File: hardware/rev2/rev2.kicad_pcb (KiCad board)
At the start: 4 copper layers, 60 x 40 mm, 154 parts, among them J1 USB_C_Receptacle_USB2.0_16P, J2 uFL, J3 uFL, J4 Antenna RF and GNSS Data, J5 Antenna GND, J6 uFL, J7 uFL, J8 Battery Connection, Q1 SS8050, SW1 SW_Push, SW2 SW_Push, U1 EClamp2522P, U2 ESP32-S3FN8, U3 SX1262IMLTRT, U4 PE4259, U5 MP2664GG-xxxx-P, U6 MAX17055ETB+, U8 TPS631000DRLR, Y1 ECS-2520SMV-400-FN-TR, Y2 TXO-20CSMV-320

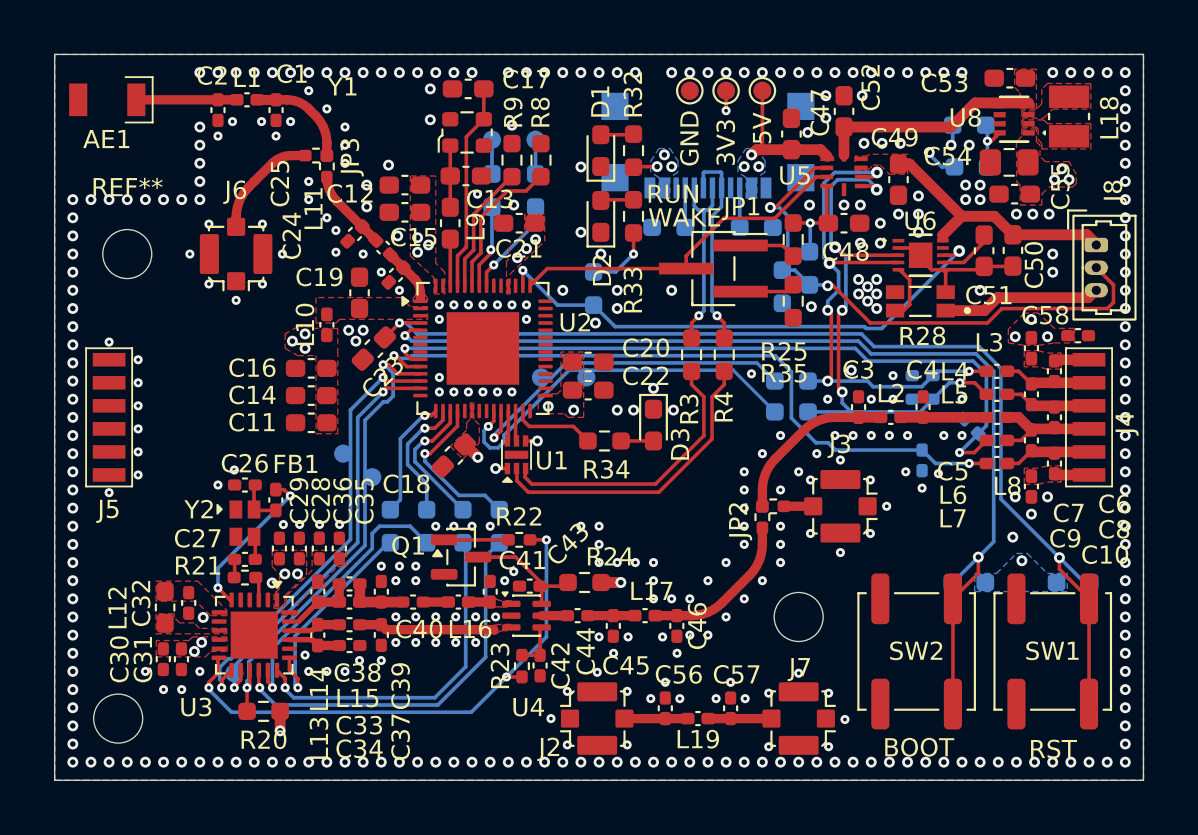
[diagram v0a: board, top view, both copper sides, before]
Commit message: fixed soldermask and silkscreen mostly
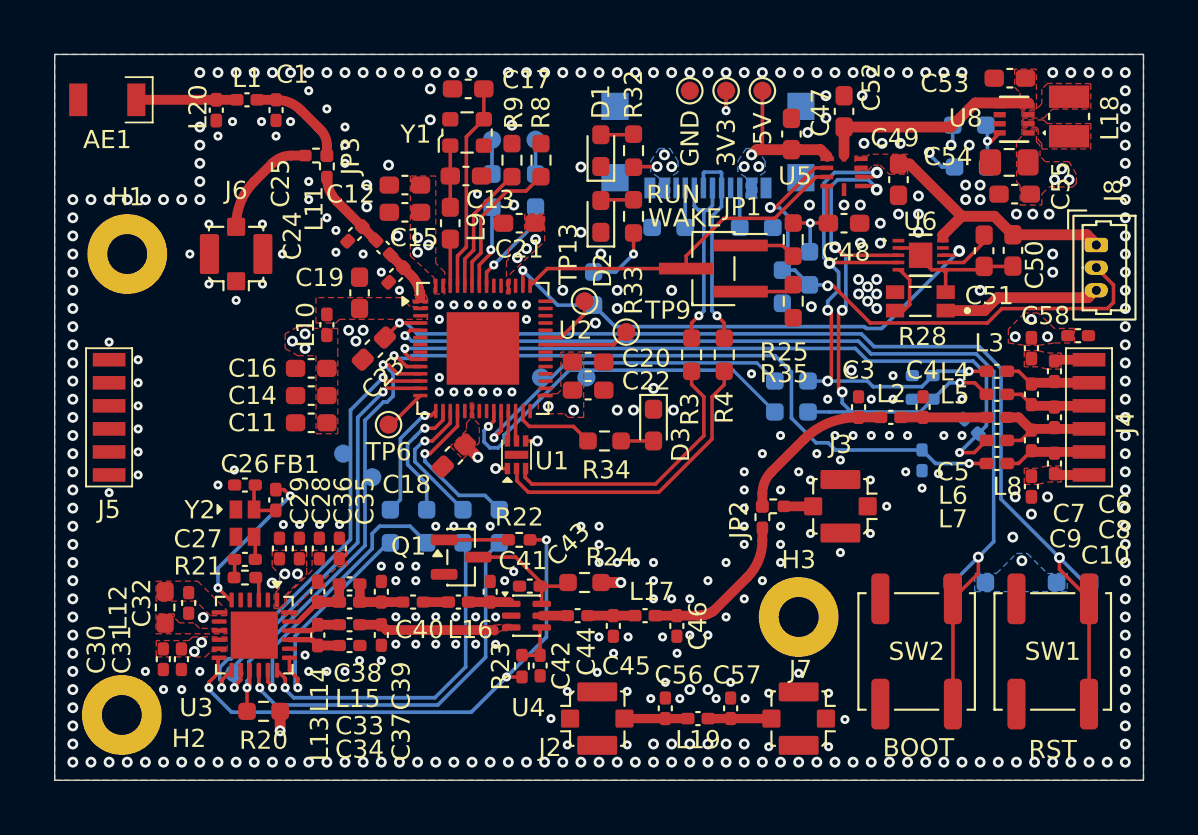
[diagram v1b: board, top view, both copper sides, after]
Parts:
- removed C2: TBD, Capacitor_SMD:C_0402_1005Metric_Pad0.74x0.62mm_HandSolder
- removed REF** (x3): MountingHole_2.7mm_M2.5, MountingHole:MountingHole_2.7mm_M2.5
- added H1: MountingHole_Pad, MountingHole:MountingHole_2.2mm_M2_Pad, F.Cu at (132.0, 68.0)
- added H2: MountingHole_Pad, MountingHole:MountingHole_2.2mm_M2_Pad, F.Cu at (131.7, 93.4)
- added H3: MountingHole_Pad, MountingHole:MountingHole_2.2mm_M2_Pad, F.Cu at (169.0, 88.0)
- added L20: 6.2 nH, Inductor_SMD:L_0402_1005Metric_Pad0.77x0.64mm_HandSolder, F.Cu at (136.9, 60.1)
- added TP13: TestPoint, TestPoint:TestPoint_Pad_D1.0mm, F.Cu at (157.2, 70.6)
- added TP6: TestPoint, TestPoint:TestPoint_Pad_D1.0mm, F.Cu at (146.4, 77.4)
- added TP9: TestPoint, TestPoint:TestPoint_Pad_D1.0mm, F.Cu at (159.5, 72.3)
- C10, C40, C44, C5, C6, C7, C8, C9: value 100 pF -> 3000 pF
- C13, C17: value TBD -> 24 pF
- C24, C25: value TBD -> 1.2 pF
- C37: value 1.33 pF -> 1.3 pF
- L1: value TBD -> 1.8 nH
- L11: value TBD -> 2.4 nH
- L15: value 17.5 nH -> 17 nH
- L3, L4, L5, L6, L7, L8: value 1.1 uH ? -> 1 uH
- R26: value 11.5kΩ -> 11.5 k
- R27: value 309kΩ -> 309 k
- R31, R35: value 10kΩ -> 10 k
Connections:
- U2 pad 14: unconnected-(U2-GPIO9-Pad14) -> Net-(U2-GPIO9)
- U2 pad 36: unconnected-(U2-SPICLK_N-Pad36) -> Net-(U2-SPICLK_N)
- U2 pad 37: unconnected-(U2-SPICLK_P-Pad37) -> Net-(U2-SPICLK_P)
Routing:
- net Net-(U2-SPICLK_N): track 0.00 -> 4.74 mm
- net Net-(U2-SPICLK_P): track 0.00 -> 3.39 mm
- net Net-(U2-GPIO9): track 0.00 -> 2.41 mm
- net /Antenna_WiFi: track 6.86 -> 5.58 mm
- net Net-(U4-RF1): track 1.18 -> 2.24 mm
- net GND: vias 416 -> 426
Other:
- board text added: "Design by: Oscar Rosenlund Teodor Sjögren Ellen Henriksson Marcus Börne Johanna Helegård Jonathan Månsby"
- board text added: "MCCX11 Group 10 Revision 2 LoRa Based Cat Tracker"
- board text removed: "MOVE TO MIDDLE"

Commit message: final edit, send to production
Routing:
- net GND: vias 426 -> 423
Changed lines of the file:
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@@
 		(capping no)
 		(filling no)
-		(zone_defaults)
 		(pcbplotparams
 			(layerselection 0x00000000_00000000_55555555_5755f5ff)
@@
 		)
 	)
-	(gr_line
+	(gr_rect
 		(start 128 57)
-		(end 128 97)
-		(stroke
-			(width 0.1)
-			(type default)
-		)
-		(layer "F.Mask")
-	)
-	(gr_line
-		(start 128 97)
 		(end 188 97)
+		(radius 1)
 		(stroke
 			(width 0.1)
-			(type default)
-		)
-		(layer "F.Mask")
-	)
-	(gr_line
-		(start 188 57)
-		(end 128 57)
-		(stroke
-			(width 0.1)
-			(type default)
-		)
-		(layer "F.Mask")
-	)
-	(gr_line
-		(start 188 57)
-		(end 188 97)
-		(stroke
-			(width 0.1)
-			(type default)
+			(type solid)
 		)
+		(fill no)
 		(layer "F.Mask")
 	)
@@
 		(start 128 57)
 		(end 188 97)
+		(radius 1)
 		(stroke
 			(width 0.05)
-			(type default)
+			(type solid)
 		)
 		(fill no)
@@
 	)
 	(via
-		(at 129 96)
-		(size 0.6)
-		(drill 0.3)
-		(layers "F.Cu" "B.Cu")
-		(free yes)
-		(net "GND")
-	)
-	(via
 		(at 168 84)
 		(size 0.5)
@@
 	)
 	(via
-		(at 187 58)
-		(size 0.6)
-		(drill 0.3)
-		(layers "F.Cu" "B.Cu")
-		(free yes)
-		(net "GND")
-	)
-	(via
 		(at 129 86)
 		(size 0.6)
@@
 	)
 	(via
-		(at 187 96)
-		(size 0.6)
-		(drill 0.3)
-		(layers "F.Cu" "B.Cu")
-		(free yes)
-		(net "GND")
-	)
-	(via
 		(at 187 67)
 		(size 0.6)
@@
 		(polygon
 			(pts
-				(xy 188 57) (xy 128 57) (xy 128 97) (xy 188 97)
+				(xy 189 56) (xy 126.987024 56.019168) (xy 127 98) (xy 189.004269 97.993696)
 			)
 		)

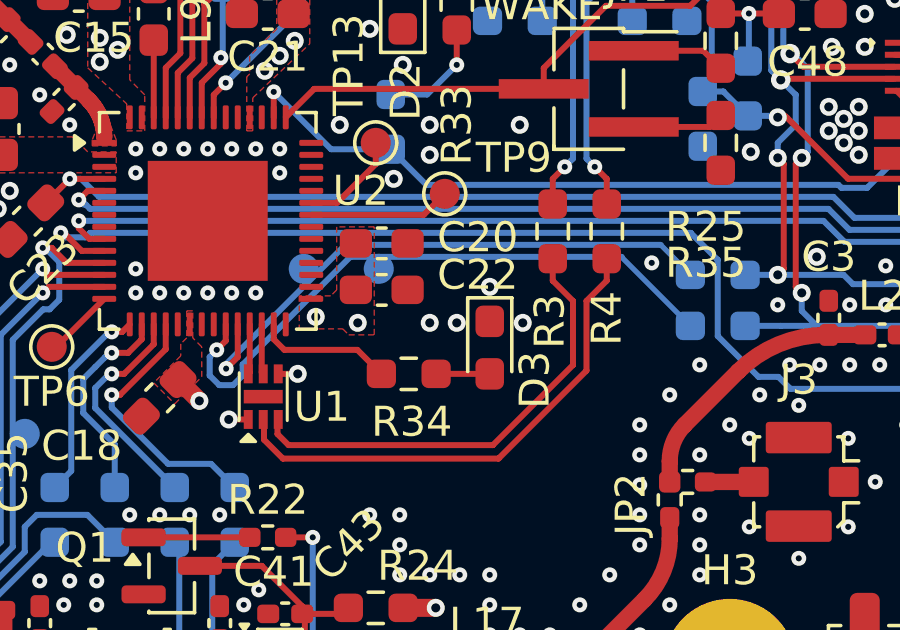
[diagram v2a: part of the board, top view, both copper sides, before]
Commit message: added resistors
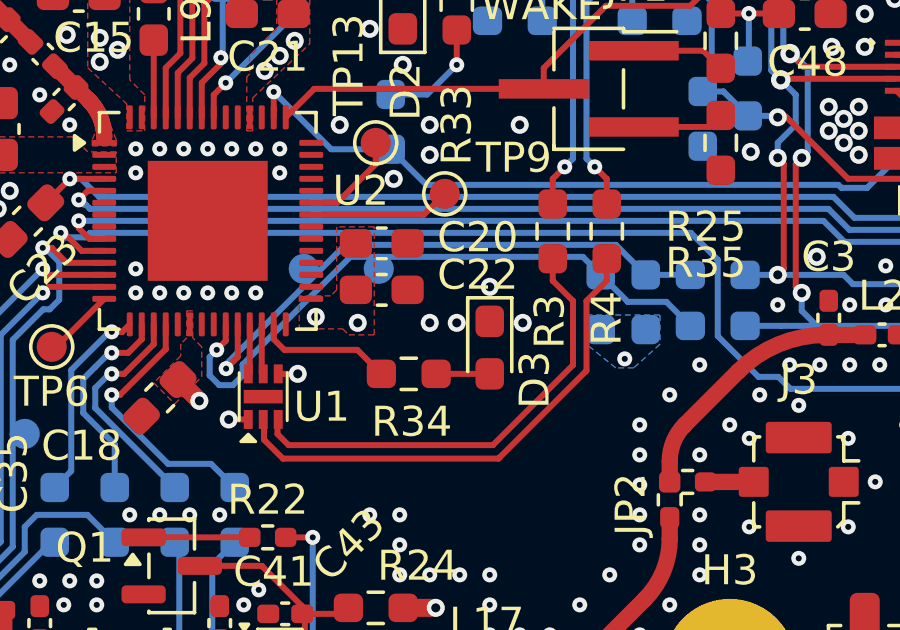
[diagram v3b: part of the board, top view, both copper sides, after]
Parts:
- added R36: 4.7 k, Resistor_SMD:R_0603_1608Metric_Pad0.98x0.95mm_HandSolder, B.Cu at (164.7, 75.9)
- added R37: 4.7 k, Resistor_SMD:R_0603_1608Metric_Pad0.98x0.95mm_HandSolder, B.Cu at (166.2, 75.9)
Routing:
- net GND: vias 423 -> 422
- net +3V3: vias 29 -> 30

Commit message: unfucked vias
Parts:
- J8: footprint Connector_Molex:Molex_PicoBlade_53047-0310_1x03_P1.25mm_Vertical -> _footprints:Unfucked_Molex_PicoBlade_53047-0310_1x03_P1.25mm_Vertical
